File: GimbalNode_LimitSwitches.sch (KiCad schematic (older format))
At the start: 22 parts

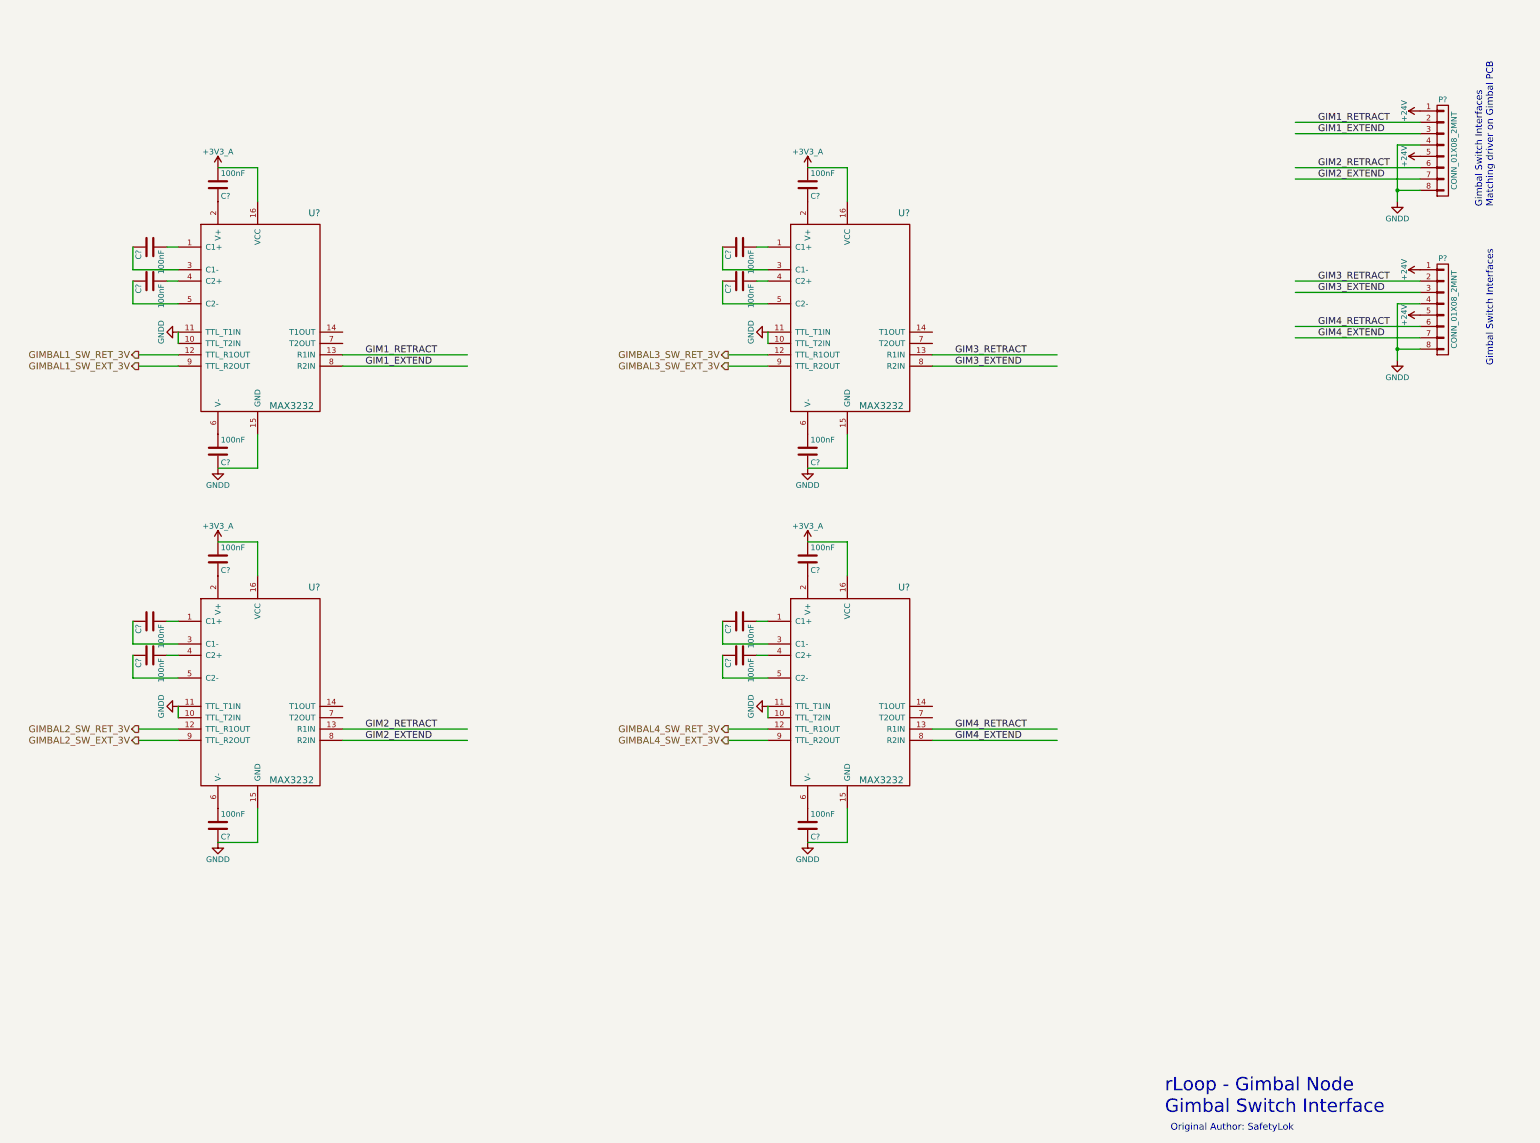
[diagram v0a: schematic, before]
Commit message: Fixup various caps on 4-20ma sheet.
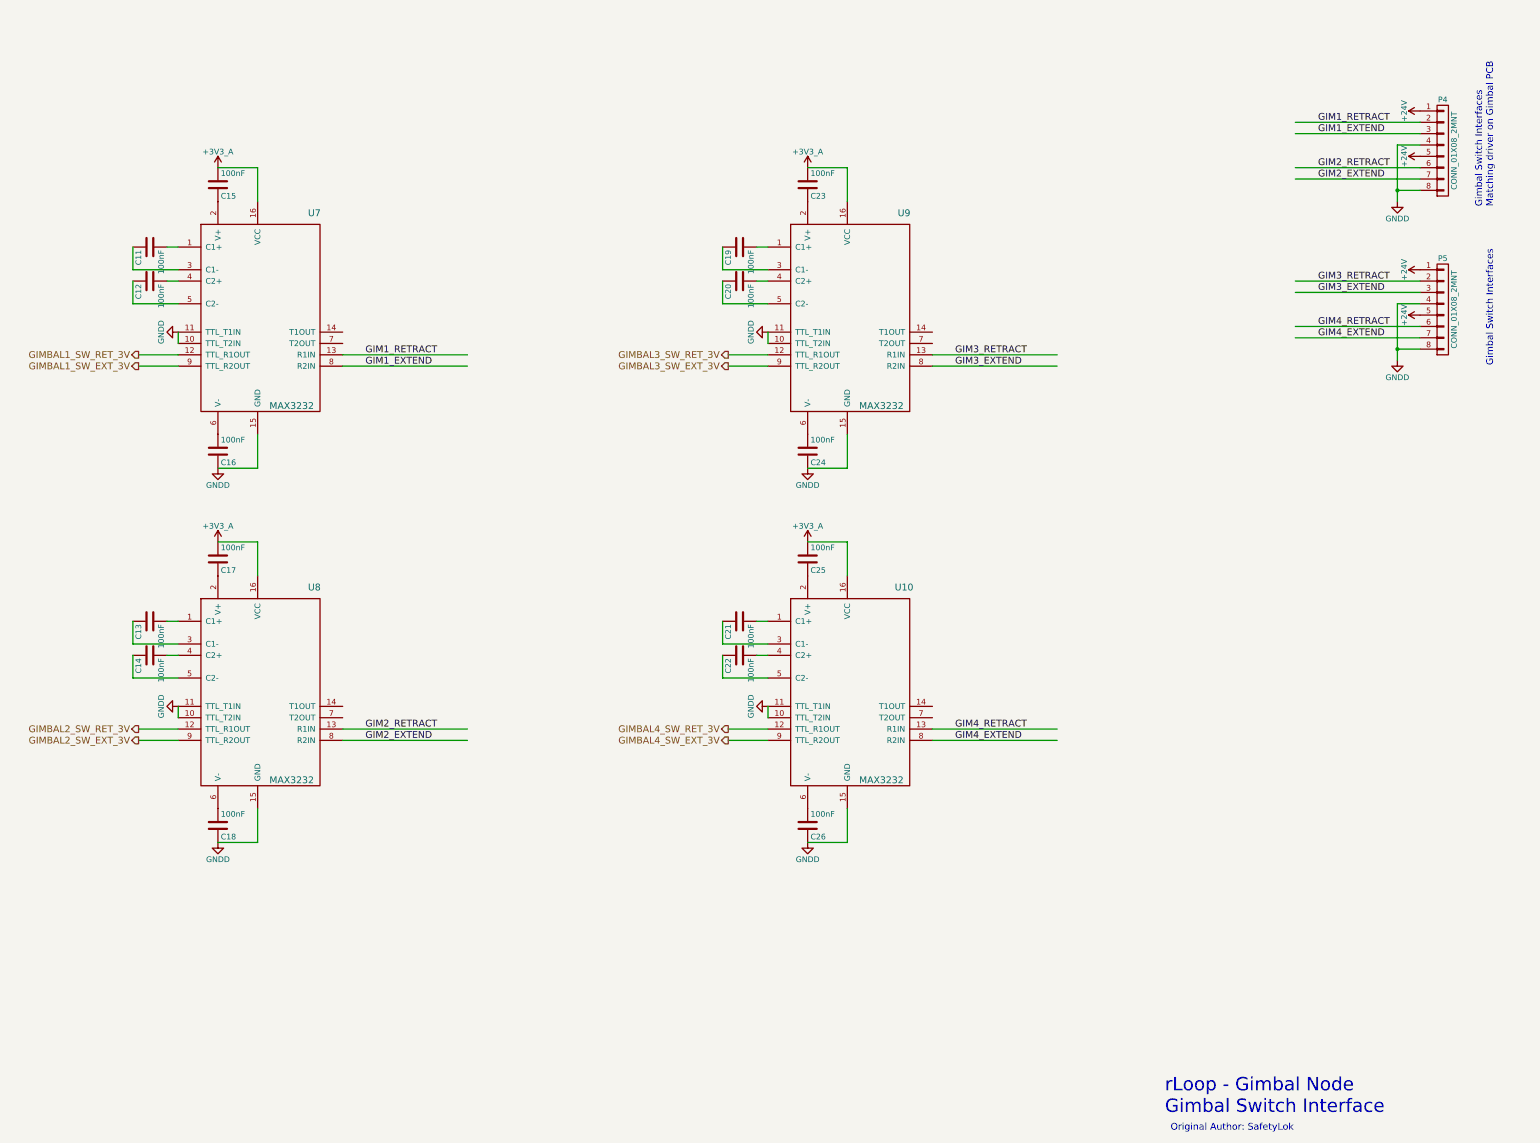
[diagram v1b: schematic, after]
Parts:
- gave numbers to parts that had none: 22
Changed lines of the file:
@@
 GIM1_EXTEND
 $Comp
-L MAX3232 U?
+L MAX3232 U7
 U 1 1 5757EC62
 P 3350 2500
-F 0 "U?" H 4350 2600 60  0000 C CNN
+F 0 "U7" H 4350 2600 60  0000 C CNN
 F 1 "MAX3232" H 4150 900 60  0000 C CNN
 F 2 "" H 3550 1900 60  0000 C CNN
@@
 $EndComp
 $Comp
-L C C?
+L C C11
 U 1 1 5757EC63
 P 2900 2700
-F 0 "C?" H 2925 2800 50  0000 L CNN
+F 0 "C11" H 2925 2800 50  0000 L CNN
 F 1 "100nF" H 2925 2600 50  0000 L CNN
 F 2 "" H 2938 2550 50  0000 C CNN
@@
 $EndComp
 $Comp
-L C C?
+L C C12
 U 1 1 5757EC64
 P 2900 3000
-F 0 "C?" H 2925 3100 50  0000 L CNN
+F 0 "C12" H 2925 3100 50  0000 L CNN
 F 1 "100nF" H 2925 2900 50  0000 L CNN
 F 2 "" H 2938 2850 50  0000 C CNN
@@
 $EndComp
 $Comp
-L C C?
+L C C15
 U 1 1 5757EC65
 P 3500 2150
-F 0 "C?" H 3525 2250 50  0000 L CNN
+F 0 "C15" H 3525 2250 50  0000 L CNN
 F 1 "100nF" H 3525 2050 50  0000 L CNN
 F 2 "" H 3538 2000 50  0000 C CNN
@@
 $EndComp
 $Comp
-L C C?
+L C C16
 U 1 1 5757EC66
 P 3500 4500
-F 0 "C?" H 3525 4600 50  0000 L CNN
+F 0 "C16" H 3525 4600 50  0000 L CNN
 F 1 "100nF" H 3525 4400 50  0000 L CNN
 F 2 "" H 3538 4350 50  0000 C CNN
@@
 $EndComp
 $Comp
-L GNDD #PWR?
+L GNDD #PWR059
 U 1 1 5757EC67
 P 3500 4650
-F 0 "#PWR?" H 3500 4400 50  0001 C CNN
+F 0 "#PWR059" H 3500 4400 50  0001 C CNN
 F 1 "GNDD" H 3500 4500 50  0000 C CNN
 F 2 "" H 3500 4650 50  0000 C CNN
@@
 	3850 4650 3850 4350
 $Comp
-L +3V3_A #PWR?
+L +3V3_A #PWR060
 U 1 1 5757EC68
 P 3500 2000
-F 0 "#PWR?" H 3500 1850 50  0001 C CNN
+F 0 "#PWR060" H 3500 1850 50  0001 C CNN
 F 1 "+3V3_A" H 3500 2140 50  0000 C CNN
 F 2 "" H 3500 2000 60  0000 C CNN
@@
 	2750 3200 2750 3000
 $Comp
-L GNDD #PWR?
+L GNDD #PWR061
 U 1 1 5757EC69
 P 3150 3450
-F 0 "#PWR?" H 3150 3200 50  0001 C CNN
+F 0 "#PWR061" H 3150 3200 50  0001 C CNN
 F 1 "GNDD" H 3150 3300 50  0000 C CNN
 F 2 "" H 3150 3450 50  0000 C CNN
@@
 	3150 3450 3150 3550
 $Comp
-L CONN_01X08_2MNT P?
+L CONN_01X08_2MNT P4
 U 1 1 5757EC6A
 P 14300 1850
-F 0 "P?" H 14300 2300 50  0000 C CNN
+F 0 "P4" H 14300 2300 50  0000 C CNN
 F 1 "CONN_01X08_2MNT" V 14400 1850 50  0000 C CNN
 F 2 "" H 14300 1850 50  0000 C CNN
@@
 Gimbal Switch Interfaces\nMatching driver on Gimbal PCB
 $Comp
-L +24V #PWR?
+L +24V #PWR062
 U 1 1 5757EC6B
 P 14100 1500
-F 0 "#PWR?" H 14100 1350 50  0001 C CNN
+F 0 "#PWR062" H 14100 1350 50  0001 C CNN
 F 1 "+24V" H 14100 1640 50  0000 C CNN
 F 2 "" H 14100 1500 50  0000 C CNN
@@
 $EndComp
 $Comp
-L +24V #PWR?
+L +24V #PWR063
 U 1 1 5757EC6C
 P 14100 1900
-F 0 "#PWR?" H 14100 1750 50  0001 C CNN
+F 0 "#PWR063" H 14100 1750 50  0001 C CNN
 F 1 "+24V" H 14100 2040 50  0000 C CNN
 F 2 "" H 14100 1900 50  0000 C CNN
@@
 $EndComp
 $Comp
-L GNDD #PWR?
+L GNDD #PWR064
 U 1 1 5757EC6D
 P 13900 2300
-F 0 "#PWR?" H 13900 2050 50  0001 C CNN
+F 0 "#PWR064" H 13900 2050 50  0001 C CNN
 F 1 "GNDD" H 13900 2150 50  0000 C CNN
 F 2 "" H 13900 2300 50  0000 C CNN
@@
 GIM2_EXTEND
 $Comp
-L CONN_01X08_2MNT P?
+L CONN_01X08_2MNT P5
 U 1 1 5757EC6E
 P 14300 3250
-F 0 "P?" H 14300 3700 50  0000 C CNN
+F 0 "P5" H 14300 3700 50  0000 C CNN
 F 1 "CONN_01X08_2MNT" V 14400 3250 50  0000 C CNN
 F 2 "" H 14300 3250 50  0000 C CNN
@@
 Gimbal Switch Interfaces
 $Comp
-L +24V #PWR?
+L +24V #PWR065
 U 1 1 5757EC6F
 P 14100 2900
-F 0 "#PWR?" H 14100 2750 50  0001 C CNN
+F 0 "#PWR065" H 14100 2750 50  0001 C CNN
 F 1 "+24V" H 14100 3040 50  0000 C CNN
 F 2 "" H 14100 2900 50  0000 C CNN
@@
 $EndComp
 $Comp
-L +24V #PWR?
+L +24V #PWR066
 U 1 1 5757EC70
 P 14100 3300
-F 0 "#PWR?" H 14100 3150 50  0001 C CNN
+F 0 "#PWR066" H 14100 3150 50  0001 C CNN
 F 1 "+24V" H 14100 3440 50  0000 C CNN
 F 2 "" H 14100 3300 50  0000 C CNN
@@
 $EndComp
 $Comp
-L GNDD #PWR?
+L GNDD #PWR067
 U 1 1 5757EC71
 P 13900 3700
-F 0 "#PWR?" H 13900 3450 50  0001 C CNN
+F 0 "#PWR067" H 13900 3450 50  0001 C CNN
 F 1 "GNDD" H 13900 3550 50  0000 C CNN
 F 2 "" H 13900 3700 50  0000 C CNN
@@
 GIM2_EXTEND
 $Comp
-L MAX3232 U?
+L MAX3232 U8
 U 1 1 5757EC72
 P 3350 5800
-F 0 "U?" H 4350 5900 60  0000 C CNN
+F 0 "U8" H 4350 5900 60  0000 C CNN
 F 1 "MAX3232" H 4150 4200 60  0000 C CNN
 F 2 "" H 3550 5200 60  0000 C CNN
@@
 $EndComp
 $Comp
-L C C?
+L C C13
 U 1 1 5757EC73
 P 2900 6000
-F 0 "C?" H 2925 6100 50  0000 L CNN
+F 0 "C13" H 2925 6100 50  0000 L CNN
 F 1 "100nF" H 2925 5900 50  0000 L CNN
 F 2 "" H 2938 5850 50  0000 C CNN
@@
 $EndComp
 $Comp
-L C C?
+L C C14
 U 1 1 5757EC74
 P 2900 6300
-F 0 "C?" H 2925 6400 50  0000 L CNN
+F 0 "C14" H 2925 6400 50  0000 L CNN
 F 1 "100nF" H 2925 6200 50  0000 L CNN
 F 2 "" H 2938 6150 50  0000 C CNN
@@
 $EndComp
 $Comp
-L C C?
+L C C17
 U 1 1 5757EC75
 P 3500 5450
-F 0 "C?" H 3525 5550 50  0000 L CNN
+F 0 "C17" H 3525 5550 50  0000 L CNN
 F 1 "100nF" H 3525 5350 50  0000 L CNN
 F 2 "" H 3538 5300 50  0000 C CNN
@@
 $EndComp
 $Comp
-L C C?
+L C C18
 U 1 1 5757EC76
 P 3500 7800
-F 0 "C?" H 3525 7900 50  0000 L CNN
+F 0 "C18" H 3525 7900 50  0000 L CNN
 F 1 "100nF" H 3525 7700 50  0000 L CNN
 F 2 "" H 3538 7650 50  0000 C CNN
@@
 $EndComp
 $Comp
-L GNDD #PWR?
+L GNDD #PWR068
 U 1 1 5757EC77
 P 3500 7950
-F 0 "#PWR?" H 3500 7700 50  0001 C CNN
+F 0 "#PWR068" H 3500 7700 50  0001 C CNN
 F 1 "GNDD" H 3500 7800 50  0000 C CNN
 F 2 "" H 3500 7950 50  0000 C CNN
@@
 	3850 7950 3850 7650
 $Comp
-L +3V3_A #PWR?
+L +3V3_A #PWR069
 U 1 1 5757EC78
 P 3500 5300
-F 0 "#PWR?" H 3500 5150 50  0001 C CNN
+F 0 "#PWR069" H 3500 5150 50  0001 C CNN
 F 1 "+3V3_A" H 3500 5440 50  0000 C CNN
 F 2 "" H 3500 5300 60  0000 C CNN
@@
 	2750 6500 2750 6300
 $Comp
-L GNDD #PWR?
+L GNDD #PWR070
 U 1 1 5757EC79
 P 3150 6750
-F 0 "#PWR?" H 3150 6500 50  0001 C CNN
+F 0 "#PWR070" H 3150 6500 50  0001 C CNN
 F 1 "GNDD" H 3150 6600 50  0000 C CNN
 F 2 "" H 3150 6750 50  0000 C CNN
@@
 GIM3_EXTEND
 $Comp
-L MAX3232 U?
+L MAX3232 U9
 U 1 1 5757EC7A
 P 8550 2500
-F 0 "U?" H 9550 2600 60  0000 C CNN
+F 0 "U9" H 9550 2600 60  0000 C CNN
 F 1 "MAX3232" H 9350 900 60  0000 C CNN
 F 2 "" H 8750 1900 60  0000 C CNN
@@
 $EndComp
 $Comp
-L C C?
+L C C19
 U 1 1 5757EC7B
 P 8100 2700
-F 0 "C?" H 8125 2800 50  0000 L CNN
+F 0 "C19" H 8125 2800 50  0000 L CNN
 F 1 "100nF" H 8125 2600 50  0000 L CNN
 F 2 "" H 8138 2550 50  0000 C CNN
@@
 $EndComp
 $Comp
-L C C?
+L C C20
 U 1 1 5757EC7C
 P 8100 3000
-F 0 "C?" H 8125 3100 50  0000 L CNN
+F 0 "C20" H 8125 3100 50  0000 L CNN
 F 1 "100nF" H 8125 2900 50  0000 L CNN
 F 2 "" H 8138 2850 50  0000 C CNN
@@
 $EndComp
 $Comp
-L C C?
+L C C23
 U 1 1 5757EC7D
 P 8700 2150
-F 0 "C?" H 8725 2250 50  0000 L CNN
+F 0 "C23" H 8725 2250 50  0000 L CNN
 F 1 "100nF" H 8725 2050 50  0000 L CNN
 F 2 "" H 8738 2000 50  0000 C CNN
@@
 $EndComp
 $Comp
-L C C?
+L C C24
 U 1 1 5757EC7E
 P 8700 4500
-F 0 "C?" H 8725 4600 50  0000 L CNN
+F 0 "C24" H 8725 4600 50  0000 L CNN
 F 1 "100nF" H 8725 4400 50  0000 L CNN
 F 2 "" H 8738 4350 50  0000 C CNN
@@
 $EndComp
 $Comp
-L GNDD #PWR?
+L GNDD #PWR071
 U 1 1 5757EC7F
 P 8700 4650
-F 0 "#PWR?" H 8700 4400 50  0001 C CNN
+F 0 "#PWR071" H 8700 4400 50  0001 C CNN
 F 1 "GNDD" H 8700 4500 50  0000 C CNN
 F 2 "" H 8700 4650 50  0000 C CNN
@@
 	9050 4650 9050 4350
 $Comp
-L +3V3_A #PWR?
+L +3V3_A #PWR072
 U 1 1 5757EC80
 P 8700 2000
-F 0 "#PWR?" H 8700 1850 50  0001 C CNN
+F 0 "#PWR072" H 8700 1850 50  0001 C CNN
 F 1 "+3V3_A" H 8700 2140 50  0000 C CNN
 F 2 "" H 8700 2000 60  0000 C CNN
@@
 	7950 3200 7950 3000
 $Comp
-L GNDD #PWR?
+L GNDD #PWR073
 U 1 1 5757EC81
 P 8350 3450
-F 0 "#PWR?" H 8350 3200 50  0001 C CNN
+F 0 "#PWR073" H 8350 3200 50  0001 C CNN
 F 1 "GNDD" H 8350 3300 50  0000 C CNN
 F 2 "" H 8350 3450 50  0000 C CNN
@@
 GIM4_EXTEND
 $Comp
-L MAX3232 U?
+L MAX3232 U10
 U 1 1 5757EC82
 P 8550 5800
-F 0 "U?" H 9550 5900 60  0000 C CNN
+F 0 "U10" H 9550 5900 60  0000 C CNN
 F 1 "MAX3232" H 9350 4200 60  0000 C CNN
 F 2 "" H 8750 5200 60  0000 C CNN
@@
 $EndComp
 $Comp
-L C C?
+L C C21
 U 1 1 5757EC83
 P 8100 6000
-F 0 "C?" H 8125 6100 50  0000 L CNN
+F 0 "C21" H 8125 6100 50  0000 L CNN
 F 1 "100nF" H 8125 5900 50  0000 L CNN
 F 2 "" H 8138 5850 50  0000 C CNN
@@
 $EndComp
 $Comp
-L C C?
+L C C22
 U 1 1 5757EC84
 P 8100 6300
-F 0 "C?" H 8125 6400 50  0000 L CNN
+F 0 "C22" H 8125 6400 50  0000 L CNN
 F 1 "100nF" H 8125 6200 50  0000 L CNN
 F 2 "" H 8138 6150 50  0000 C CNN
@@
 $EndComp
 $Comp
-L C C?
+L C C25
 U 1 1 5757EC85
 P 8700 5450
-F 0 "C?" H 8725 5550 50  0000 L CNN
+F 0 "C25" H 8725 5550 50  0000 L CNN
 F 1 "100nF" H 8725 5350 50  0000 L CNN
 F 2 "" H 8738 5300 50  0000 C CNN
@@
 $EndComp
 $Comp
-L C C?
+L C C26
 U 1 1 5757EC86
 P 8700 7800
-F 0 "C?" H 8725 7900 50  0000 L CNN
+F 0 "C26" H 8725 7900 50  0000 L CNN
 F 1 "100nF" H 8725 7700 50  0000 L CNN
 F 2 "" H 8738 7650 50  0000 C CNN
@@
 $EndComp
 $Comp
-L GNDD #PWR?
+L GNDD #PWR074
 U 1 1 5757EC87
 P 8700 7950
-F 0 "#PWR?" H 8700 7700 50  0001 C CNN
+F 0 "#PWR074" H 8700 7700 50  0001 C CNN
 F 1 "GNDD" H 8700 7800 50  0000 C CNN
 F 2 "" H 8700 7950 50  0000 C CNN
@@
 	9050 7950 9050 7650
 $Comp
-L +3V3_A #PWR?
+L +3V3_A #PWR075
 U 1 1 5757EC88
 P 8700 5300
-F 0 "#PWR?" H 8700 5150 50  0001 C CNN
+F 0 "#PWR075" H 8700 5150 50  0001 C CNN
 F 1 "+3V3_A" H 8700 5440 50  0000 C CNN
 F 2 "" H 8700 5300 60  0000 C CNN
@@
 	7950 6500 7950 6300
 $Comp
-L GNDD #PWR?
+L GNDD #PWR076
 U 1 1 5757EC89
 P 8350 6750
-F 0 "#PWR?" H 8350 6500 50  0001 C CNN
+F 0 "#PWR076" H 8350 6500 50  0001 C CNN
 F 1 "GNDD" H 8350 6600 50  0000 C CNN
 F 2 "" H 8350 6750 50  0000 C CNN

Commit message: Fixup 5V to 3V connections
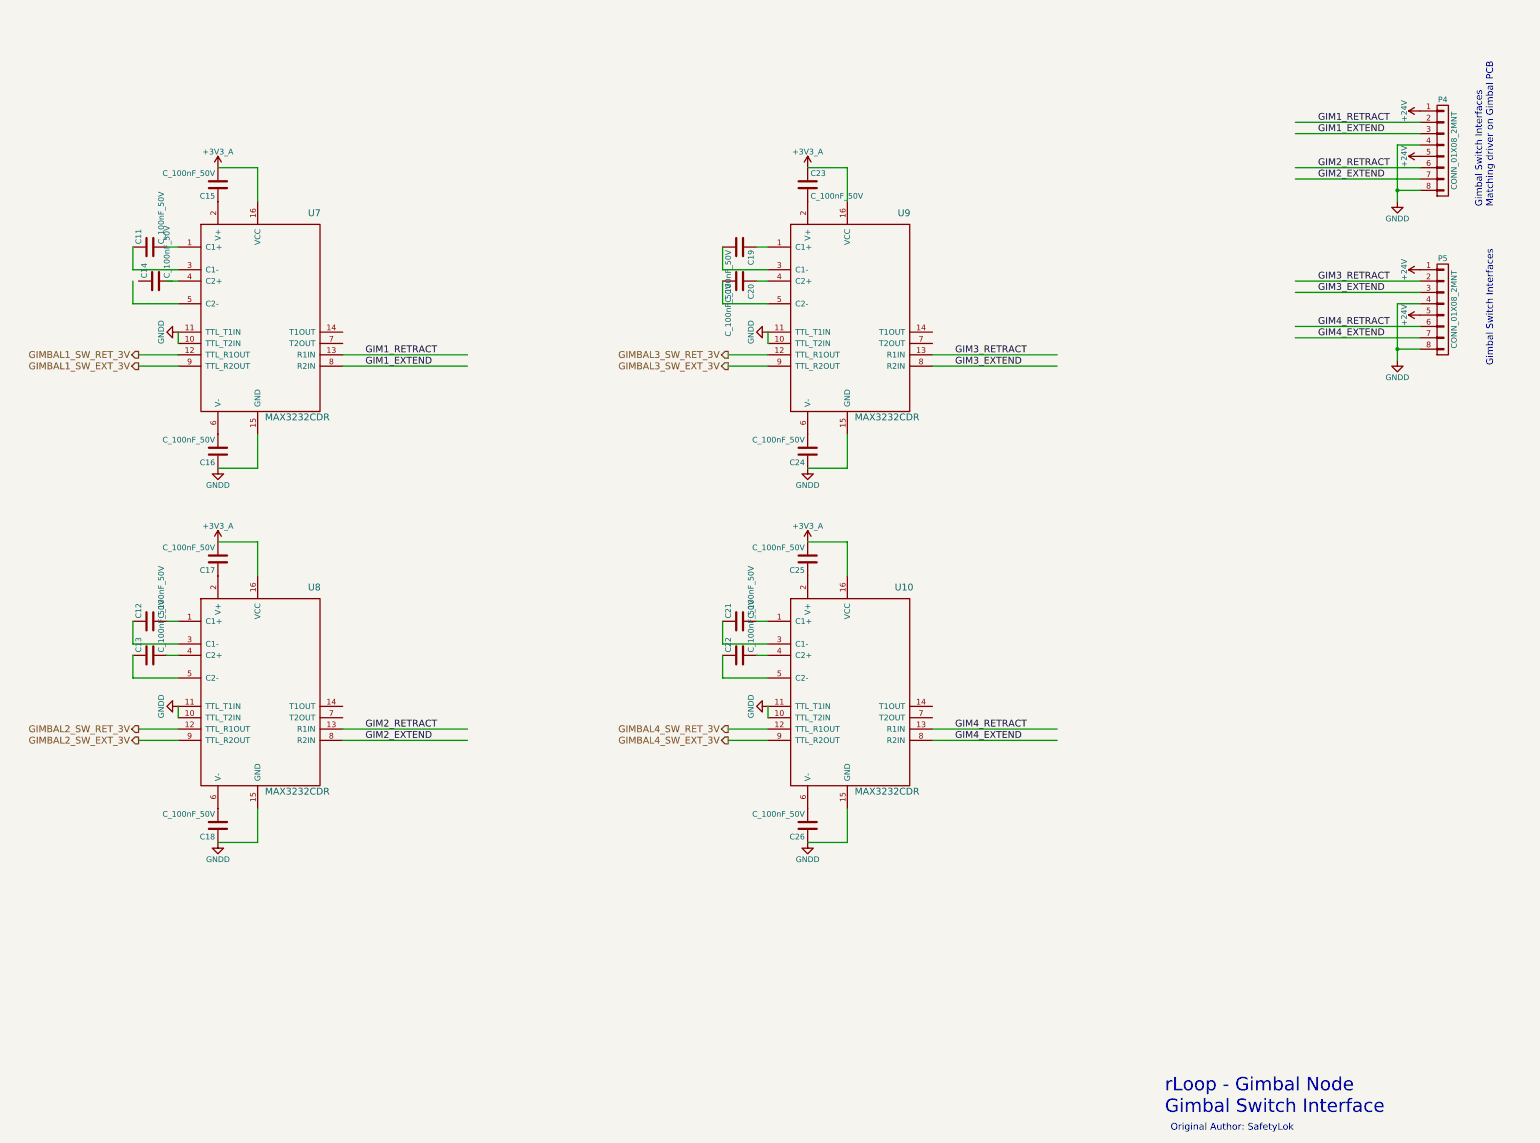
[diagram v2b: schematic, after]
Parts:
- removed C11, C12, C13, C14, C15, C16, C17, C18, C19, C20, C21, C22, C23, C24, C25, C26: 100nF, symbol C
- removed U10, U7, U8, U9: MAX3232, symbol MAX3232
- added C11, C12, C13, C14, C15, C16, C17, C18, C19, C20, C21, C22, C23, C24, C25, C26: C_100nF_50V, RLOOP_FOOTPRINTS:rLoop_C_0603, symbol C_100nF_50V
- added U10, U7, U8, U9: MAX3232CDR, RLOOP_FOOTPRINTS:rLoop_SOIC_16, symbol MAX3232CDR
